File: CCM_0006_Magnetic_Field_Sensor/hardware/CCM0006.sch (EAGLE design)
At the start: 28 parts, among them IC1 AD654, IC2 AD820R, IC3 AD820R

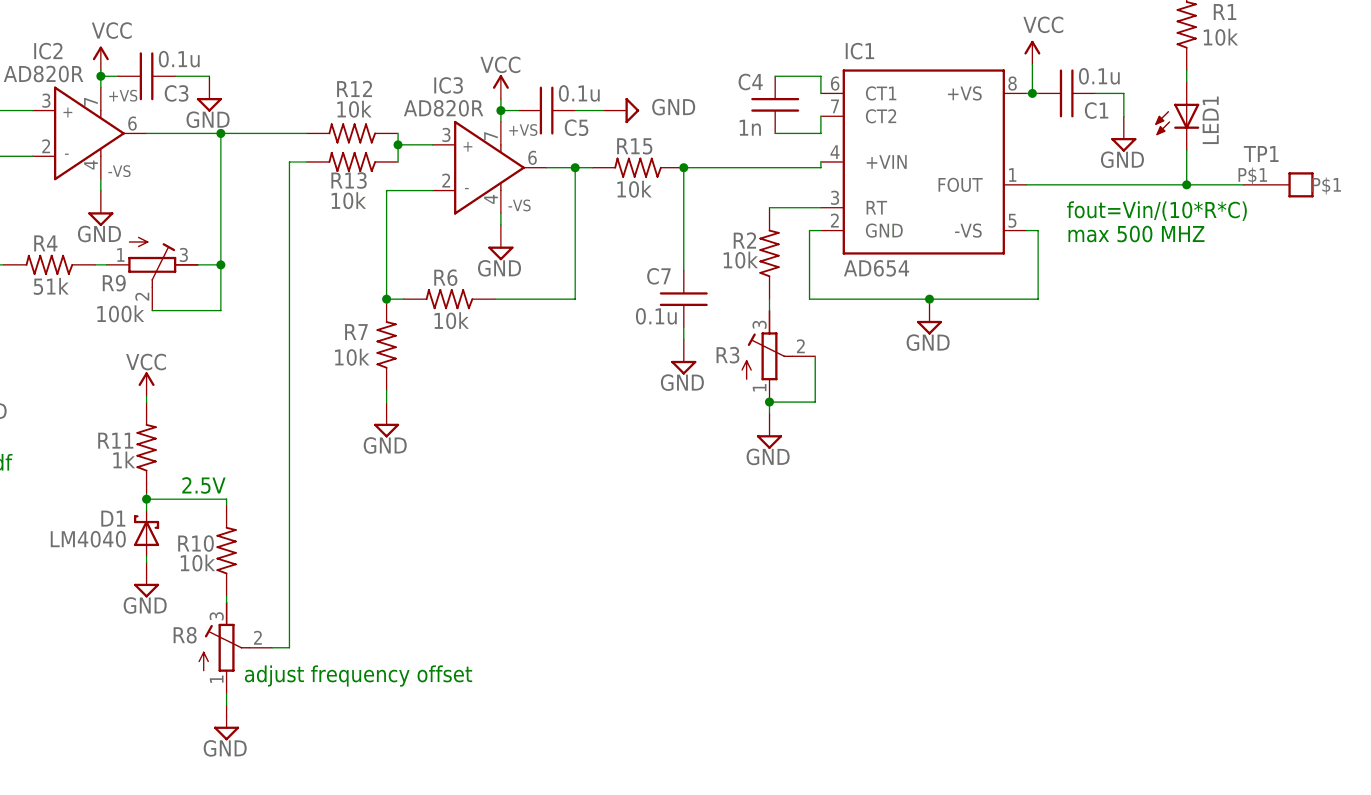
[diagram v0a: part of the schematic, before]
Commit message: fixed stepper motor firmware bug with parameter saving (v1.5)
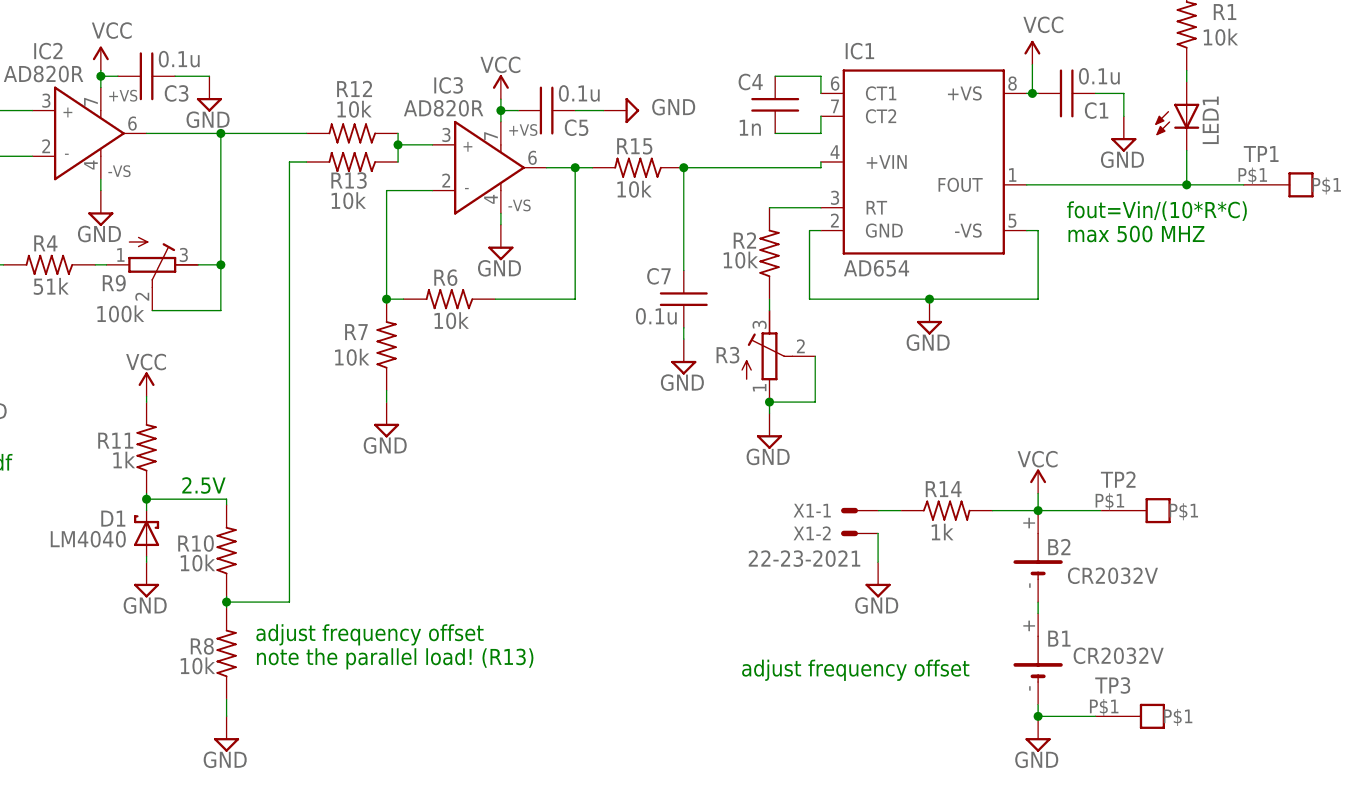
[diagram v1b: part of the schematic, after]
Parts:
- added B1, B2: CR2032V, battery:CR2032V
- added R14: 1k, noah:RESISTOR2512
- added TP2, TP3: TESTPOINT, Fitch:TESTPOINT
- added X1: 22-23-2021, con-molex:22-23-2021
- R8: value (none) -> 10k; device rcl:R-TRIMM74W -> ic:RESISTOR0603
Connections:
- removed net N$19: R13.2, R8.S
- new net N$20: B1.+, B2.-
- new net N$21: R14.1, X1-1.S
- net AGND: now also B1.-, R8.1, TP3.P$1, X1-2.S; no longer R8.A
- net N$11: now also R13.2, R8.2; no longer R8.E
- net VCC: now also B2.+, R14.2, TP2.P$1
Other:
- note added: "adjust frequency offset note the parallel load! (R13)"
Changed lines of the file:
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@@
 <setting verticaltext="up"/>
 </settings>
-<grid distance="0.1" unitdist="inch" unit="inch" style="lines" multiple="1" display="no" altdistance="0.01" altunitdist="inch" altunit="inch"/>
+<grid distance="0.025" unitdist="inch" unit="inch" style="lines" multiple="1" display="no" altdistance="0.01" altunitdist="inch" altunit="inch"/>
 <layers>
 <layer number="1" name="Top" color="4" fill="1" visible="no" active="no"/>
@@
 <part name="R5" library="ic" deviceset="RESISTOR" device="0603" value="1k"/>
 <part name="SUPPLY6" library="supply2" deviceset="AGND" device="" value="GND"/>
-<part name="R8" library="rcl" deviceset="R-TRIMM" device="74W"/>
 <part name="R10" library="ic" deviceset="RESISTOR" device="0603" value="10k"/>
 <part name="D1" library="Fitch" deviceset="LM4040" device=""/>
@@
 <part name="C7" library="ic" deviceset="CAPACITOR" device="0603" value="0.1u"/>
 <part name="SUPPLY15" library="supply2" deviceset="AGND" device="" value="GND"/>
+<part name="B1" library="battery" deviceset="CR2032V" device=""/>
+<part name="B2" library="battery" deviceset="CR2032V" device=""/>
+<part name="SUPPLY16" library="supply2" deviceset="AGND" device="" value="GND"/>
+<part name="P+7" library="SparkFun" deviceset="VCC" device=""/>
+<part name="TP2" library="Fitch" deviceset="TESTPOINT" device=""/>
+<part name="TP3" library="Fitch" deviceset="TESTPOINT" device=""/>
+<part name="X1" library="con-molex" deviceset="22-23-2021" device=""/>
+<part name="R14" library="noah" deviceset="RESISTOR" device="2512" value="1k"/>
+<part name="SUPPLY17" library="supply2" deviceset="AGND" device="" value="GND"/>
+<part name="R8" library="ic" deviceset="RESISTOR" device="0603" value="10k"/>
 </parts>
 <sheets>
@@
 <plain>
 <text x="127" y="77.47" size="1.778" layer="91">2.5V</text>
-<text x="133.985" y="56.515" size="1.778" layer="91">adjust frequency offset</text>
+<text x="135.255" y="58.42" size="1.778" layer="91">adjust frequency offset
+note the parallel load! (R13)</text>
 <text x="9.525" y="80.01" size="1.778" layer="91">single supply absolute value circuit, see
 http://www.analog.com/library/analogDialogue/archives/44-04/absolute.html/absolute.pdf</text>
@@
 max 500 MHZ</text>
 <text x="58.42" y="58.42" size="2.54" layer="91">NEEDS BATTERY POWER &gt;5V</text>
+<text x="189.23" y="57.15" size="1.778" layer="91">adjust frequency offset</text>
 </plain>
 <instances>
@@
 </instance>
 <instance part="SUPPLY6" gate="G$1" x="105.41" y="88.9"/>
-<instance part="R8" gate="G$1" x="132.08" y="60.325" smashed="yes">
-<attribute name="NAME" x="128.905" y="62.611" size="1.778" layer="95" rot="R180"/>
-<attribute name="VALUE" x="128.27" y="56.515" size="1.778" layer="96" rot="R90"/>
-</instance>
 <instance part="R10" gate="G$1" x="132.08" y="71.12" smashed="yes" rot="R90">
 <attribute name="NAME" x="130.81" y="72.7964" size="1.778" layer="95" rot="R180"/>
@@
 </instance>
 <instance part="SUPPLY8" gate="G$1" x="123.19" y="67.31"/>
-<instance part="SUPPLY7" gate="G$1" x="132.08" y="51.435"/>
+<instance part="SUPPLY7" gate="G$1" x="132.08" y="50.165"/>
 <instance part="U$1" gate="G$1" x="68.58" y="133.985"/>
 <instance part="JP1" gate="A" x="13.335" y="140.335" rot="R90"/>
@@
 </instance>
 <instance part="SUPPLY15" gate="G$1" x="182.88" y="92.075"/>
+<instance part="B1" gate="1" x="222.25" y="59.055" smashed="yes" rot="R90">
+<attribute name="NAME" x="226.06" y="62.23" size="1.778" layer="95" rot="R180"/>
+<attribute name="VALUE" x="236.22" y="60.325" size="1.778" layer="96" rot="R180"/>
+</instance>
+<instance part="B2" gate="1" x="222.25" y="70.485" smashed="yes" rot="R90">
+<attribute name="NAME" x="226.06" y="72.39" size="1.778" layer="95" rot="R180"/>
+<attribute name="VALUE" x="235.585" y="69.215" size="1.778" layer="96" rot="R180"/>
+</instance>
+<instance part="SUPPLY16" gate="G$1" x="222.25" y="50.165"/>
+<instance part="P+7" gate="1" x="222.25" y="77.47" smashed="yes">
+<attribute name="VALUE" x="219.964" y="80.391" size="1.778" layer="96"/>
+</instance>
+<instance part="TP2" gate="G$1" x="234.315" y="75.565"/>
+<instance part="TP3" gate="G$1" x="233.68" y="52.705"/>
+<instance part="X1" gate="-1" x="201.93" y="75.565" smashed="yes" rot="MR0">
+<attribute name="NAME" x="199.39" y="74.803" size="1.524" layer="95" rot="MR0"/>
+<attribute name="VALUE" x="202.692" y="69.342" size="1.778" layer="96" rot="MR0"/>
+</instance>
+<instance part="X1" gate="-2" x="201.93" y="73.025" smashed="yes" rot="MR0">
+<attribute name="NAME" x="199.39" y="72.263" size="1.524" layer="95" rot="MR0"/>
+</instance>
+<instance part="R14" gate="G$1" x="212.09" y="75.565" smashed="yes">
+<attribute name="NAME" x="209.55" y="77.0636" size="1.778" layer="95"/>
+<attribute name="VALUE" x="210.185" y="72.263" size="1.778" layer="96"/>
+</instance>
+<instance part="SUPPLY17" gate="G$1" x="204.47" y="67.31"/>
+<instance part="R8" gate="G$1" x="132.08" y="59.69" smashed="yes" rot="R90">
+<attribute name="NAME" x="130.81" y="61.3664" size="1.778" layer="95" rot="R180"/>
+<attribute name="VALUE" x="130.81" y="59.182" size="1.778" layer="96" rot="R180"/>
+</instance>
 </instances>
 <busses>
@@
 </segment>
 <segment>
-<pinref part="R8" gate="G$1" pin="A"/>
-<pinref part="SUPPLY7" gate="G$1" pin="AGND"/>
-<wire x1="132.08" y1="53.975" x2="132.08" y2="55.245" width="0.1524" layer="91"/>
-</segment>
-<segment>
 <pinref part="C2" gate="G$1" pin="2"/>
 <pinref part="SUPPLY9" gate="G$1" pin="AGND"/>
@@
 <pinref part="C7" gate="G$1" pin="1"/>
 <wire x1="182.88" y1="94.615" x2="182.88" y2="95.885" width="0.1524" layer="91"/>
+</segment>
+<segment>
+<pinref part="SUPPLY16" gate="G$1" pin="AGND"/>
+<pinref part="B1" gate="1" pin="-"/>
+<wire x1="222.25" y1="52.705" x2="222.25" y2="53.975" width="0.1524" layer="91"/>
+<pinref part="TP3" gate="G$1" pin="P$1"/>
+<wire x1="228.6" y1="52.705" x2="222.25" y2="52.705" width="0.1524" layer="91"/>
+<junction x="222.25" y="52.705"/>
+</segment>
+<segment>
+<pinref part="X1" gate="-2" pin="S"/>
+<pinref part="SUPPLY17" gate="G$1" pin="AGND"/>
+<wire x1="204.47" y1="73.025" x2="204.47" y2="69.85" width="0.1524" layer="91"/>
+</segment>
+<segment>
+<pinref part="SUPPLY7" gate="G$1" pin="AGND"/>
+<pinref part="R8" gate="G$1" pin="1"/>
+<wire x1="132.08" y1="52.705" x2="132.08" y2="54.61" width="0.1524" layer="91"/>
 </segment>
 </net>
@@
 <wire x1="164.465" y1="120.015" x2="162.56" y2="120.015" width="0.1524" layer="91"/>
 <junction x="162.56" y="120.015"/>
+</segment>
+<segment>
+<pinref part="B2" gate="1" pin="+"/>
+<pinref part="P+7" gate="1" pin="VCC"/>
+<wire x1="222.25" y1="75.565" x2="222.25" y2="77.47" width="0.1524" layer="91"/>
+<pinref part="TP2" gate="G$1" pin="P$1"/>
+<wire x1="229.235" y1="75.565" x2="222.25" y2="75.565" width="0.1524" layer="91"/>
+<junction x="222.25" y="75.565"/>
+<pinref part="R14" gate="G$1" pin="2"/>
+<wire x1="222.25" y1="75.565" x2="217.17" y2="75.565" width="0.1524" layer="91"/>
 </segment>
 </net>
@@
 <net name="N$11" class="0">
 <segment>
-<pinref part="R8" gate="G$1" pin="E"/>
 <pinref part="R10" gate="G$1" pin="1"/>
 <wire x1="132.08" y1="65.405" x2="132.08" y2="66.04" width="0.1524" layer="91"/>
+<pinref part="R13" gate="G$1" pin="2"/>
+<wire x1="139.065" y1="65.405" x2="139.065" y2="114.3" width="0.1524" layer="91"/>
+<wire x1="139.065" y1="114.3" x2="140.97" y2="114.3" width="0.1524" layer="91"/>
+<wire x1="132.08" y1="65.405" x2="139.065" y2="65.405" width="0.1524" layer="91"/>
+<pinref part="R8" gate="G$1" pin="2"/>
+<wire x1="132.08" y1="64.77" x2="132.08" y2="65.405" width="0.1524" layer="91"/>
+<junction x="132.08" y="65.405"/>
 </segment>
 </net>
@@
 </segment>
 </net>
-<net name="N$19" class="0">
-<segment>
-<pinref part="R8" gate="G$1" pin="S"/>
-<wire x1="137.16" y1="60.325" x2="139.065" y2="60.325" width="0.1524" layer="91"/>
-<wire x1="139.065" y1="60.325" x2="139.065" y2="114.3" width="0.1524" layer="91"/>
-<pinref part="R13" gate="G$1" pin="2"/>
-<wire x1="139.065" y1="114.3" x2="140.97" y2="114.3" width="0.1524" layer="91"/>
-</segment>
-</net>
 <net name="N$10" class="0">
 <segment>
@@
 </segment>
 </net>
+<net name="N$20" class="0">
+<segment>
+<pinref part="B1" gate="1" pin="+"/>
+<pinref part="B2" gate="1" pin="-"/>
+<wire x1="222.25" y1="64.135" x2="222.25" y2="65.405" width="0.1524" layer="91"/>
+</segment>
+</net>
+<net name="N$21" class="0">
+<segment>
+<pinref part="X1" gate="-1" pin="S"/>
+<pinref part="R14" gate="G$1" pin="1"/>
+<wire x1="204.47" y1="75.565" x2="207.01" y2="75.565" width="0.1524" layer="91"/>
+</segment>
+</net>
